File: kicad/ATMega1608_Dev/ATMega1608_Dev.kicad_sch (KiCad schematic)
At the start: 36 parts, among them J1 Alt Power, J2 USB_B_Micro, J3 Power OUT, J4 Comm, J5 GPIO1, J6 GPIO2, SW1 RESET, U1 MCP1700-3302E_SOT23, U2 FT232RQ, U3 ATMega1608_32

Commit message: Schematic complete
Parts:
- added H1, H2: MountingHole, MountingHole:MountingHole_2.7mm_M2.5, symbol Mechanical:MountingHole
- added LG1, LG2: logo, mech:MyBasic_rounded_50_1, symbol mech:logo
- added LG3: logo, Symbol:KiCad-Logo_5mm_SilkScreen, symbol mech:logo
- C7: renamed from C4; value C -> 100nF
- C8: renamed from C3; value C -> 100nF
- D5: renamed from D1; value D -> PESD3V3S1UB; footprint (none) -> Diode_SMD:D_SOD-523
- R2, R7, R8: value R -> 270Ω
- R9: renamed from R1; value R -> 10kΩ
- renumbered C5 to C1, C6 to C2, C7 to C3, C8 to C4, C1 to C5, C2 to C6, D2 to D1, D4 to D2, D5 to D4, J4 to J3, J5 to J4, J6 to J5, J3 to J6, R11 to R1, R9 to R10, R10 to R11
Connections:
- net +5V: now reaches C5.1, D1.1 (K), D2.1 (K), U1.3 (VI)
- net +3.3V renamed +3V3
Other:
- note added: "5mA"
- moved on the sheet: C1, C2, C3, C4, C5, C6, C7, C8, D1, D2, D3, D4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

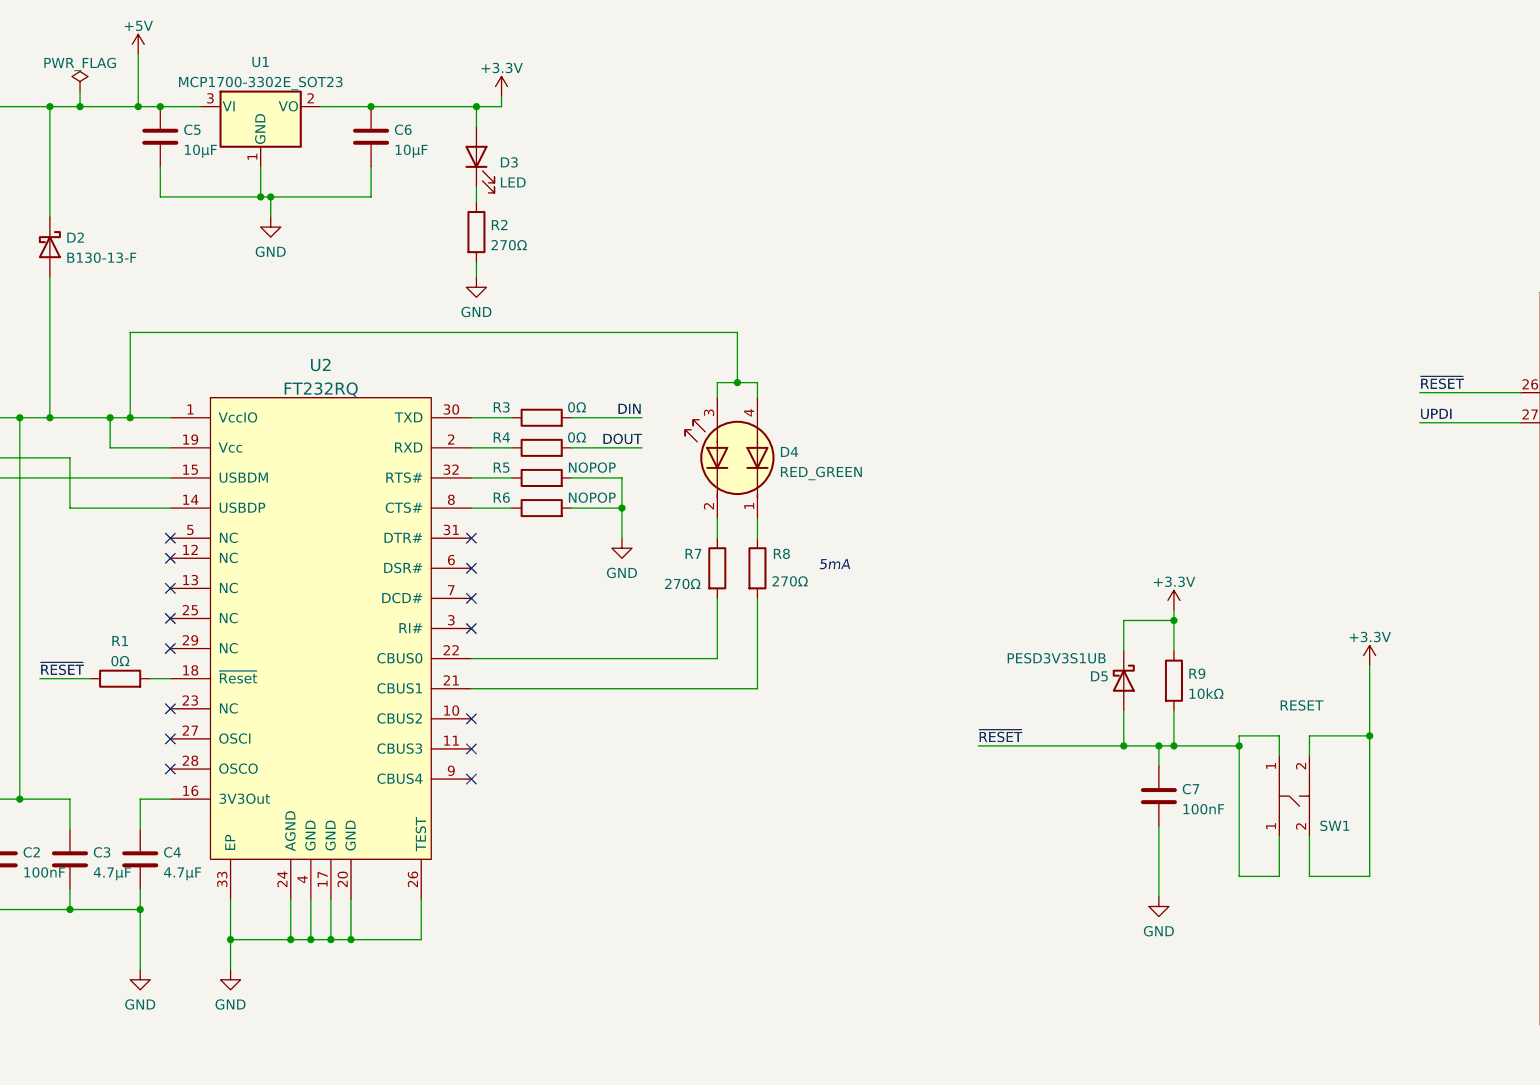
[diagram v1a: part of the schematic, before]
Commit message: Started on the layout
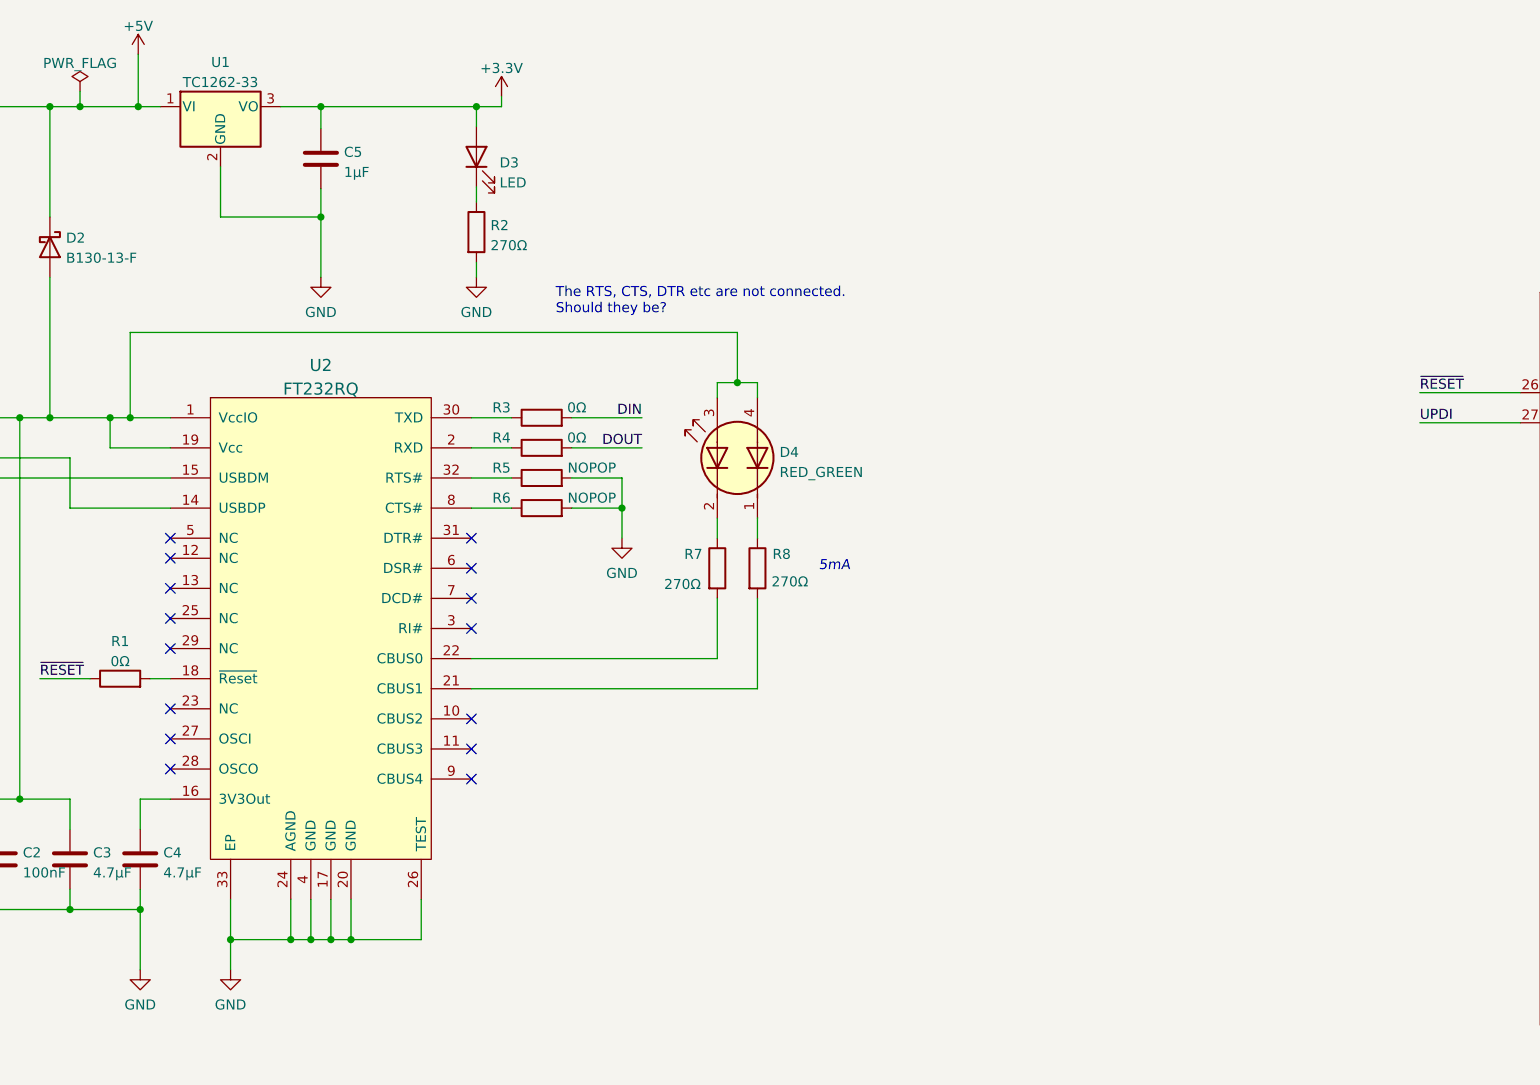
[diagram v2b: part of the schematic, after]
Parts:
- removed C6: 10μF, Capacitor_SMD:C_1210_3225Metric, symbol Device:C
- removed C7: 100nF, Capacitor_SMD:C_0805_2012Metric, symbol Device:C
- removed D5: PESD3V3S1UB, Diode_SMD:D_SOD-523, symbol Device:D_Schottky
- removed R9: 10kΩ, Resistor_SMD:R_0805_2012Metric, symbol Device:R
- removed SW1: RESET, Button_Switch_SMD:SW_SPST_Omron_B3FS-100xP, symbol attiny13_breakout:B3S-1000
- removed U1: MCP1700-3302E_SOT23, Package_TO_SOT_SMD:SOT-23, symbol Regulator_Linear:MCP1700-3302E_SOT23
- added U1: TC1262-33, Package_TO_SOT_SMD:SOT-223-3_TabPin2, symbol Regulator_Linear:TC1262-33
- C5: value 10μF -> 1μF; footprint Capacitor_SMD:C_1210_3225Metric -> Capacitor_SMD:C_0805_2012Metric_Pad1.18x1.45mm_HandSolder
- D4: footprint LED_SMD:LED_1210_3225Metric -> atmega1608_footprints:LED_KKAA_15-22SURSYGC
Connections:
- net +3V3: now also C5.1, U1.3 (VO)
- net +5V: now also U1.1 (VI); no longer C5.1
- net GND: now also U1.2 (GND)
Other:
- note added: "The RTS, CTS, DTR etc are not connected. Should they be?"

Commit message: The layout is complete - pending verification of USB interface
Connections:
- net DIN: now also J4.1 (Pin_1); no longer J4.2 (Pin_2)
- net DOUT: now also J4.2 (Pin_2); no longer J4.1 (Pin_1)
- net PF0: now also J5.10 (Pin_10); no longer J5.5 (Pin_5)
- net PF1: now also J5.9 (Pin_9); no longer J5.6 (Pin_6)
- net PF2: now also J5.8 (Pin_8); no longer J5.7 (Pin_7)
- net PF3: now also J5.7 (Pin_7); no longer J5.8 (Pin_8)
- net PF4: now also J5.6 (Pin_6); no longer J5.9 (Pin_9)
- net PF5: now also J5.5 (Pin_5); no longer J5.10 (Pin_10)
- net RxD0: now also J3.2 (Pin_2); no longer J3.4 (Pin_4)
- net SCL: now also J3.4 (Pin_4); no longer J3.2 (Pin_2)
- net SDA: now also J3.3 (Pin_3); no longer J3.1 (Pin_1)
- net TxD0: now also J3.1 (Pin_1); no longer J3.3 (Pin_3)
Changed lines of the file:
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@@
     (stroke (width 0) (type default) (color 0 0 0 0))
   )
-  (wire (pts (xy 165.227 193.675) (xy 174.752 193.675))
+  (wire (pts (xy 165.227 193.548) (xy 174.752 193.548))
     (stroke (width 0) (type default) (color 0 0 0 0))
   )
@@
     (stroke (width 0) (type default) (color 0 0 0 0))
   )
-  (wire (pts (xy 165.227 186.055) (xy 174.752 186.055))
+  (wire (pts (xy 165.227 185.928) (xy 174.752 185.928))
     (stroke (width 0) (type default) (color 0 0 0 0))
   )
@@
     (stroke (width 0) (type default) (color 0 0 0 0))
   )
-  (wire (pts (xy 165.227 198.755) (xy 174.752 198.755))
+  (wire (pts (xy 165.227 198.628) (xy 174.752 198.628))
     (stroke (width 0) (type default) (color 0 0 0 0))
   )
@@
     (stroke (width 0) (type default) (color 0 0 0 0))
   )
-  (wire (pts (xy 165.227 188.595) (xy 174.752 188.595))
+  (wire (pts (xy 165.227 188.468) (xy 174.752 188.468))
     (stroke (width 0) (type default) (color 0 0 0 0))
   )
@@
     (stroke (width 0) (type default) (color 0 0 0 0))
   )
-  (wire (pts (xy 165.227 180.975) (xy 174.752 180.975))
+  (wire (pts (xy 165.227 180.848) (xy 174.752 180.848))
     (stroke (width 0) (type default) (color 0 0 0 0))
   )
@@
     (stroke (width 0) (type default) (color 0 0 0 0))
   )
-  (wire (pts (xy 165.227 183.515) (xy 174.752 183.515))
+  (wire (pts (xy 165.227 183.388) (xy 174.752 183.388))
     (stroke (width 0) (type default) (color 0 0 0 0))
   )
@@
     (stroke (width 0) (type default) (color 0 0 0 0))
   )
-  (wire (pts (xy 165.227 191.135) (xy 174.752 191.135))
+  (wire (pts (xy 165.227 191.008) (xy 174.752 191.008))
     (stroke (width 0) (type default) (color 0 0 0 0))
   )
@@
     (stroke (width 0) (type default) (color 0 0 0 0))
   )
-  (wire (pts (xy 165.227 196.215) (xy 174.752 196.215))
+  (wire (pts (xy 165.227 196.088) (xy 174.752 196.088))
     (stroke (width 0) (type default) (color 0 0 0 0))
   )
@@
     (effects (font (size 1.27 1.27)) (justify right bottom))
   )
-  (label "SDA" (at 174.752 180.975 180)
-    (effects (font (size 1.27 1.27)) (justify right bottom))
-  )
-  (label "SS" (at 174.752 198.755 180)
+  (label "SDA" (at 174.752 185.928 180)
+    (effects (font (size 1.27 1.27)) (justify right bottom))
+  )
+  (label "SS" (at 174.752 198.628 180)
     (effects (font (size 1.27 1.27)) (justify right bottom))
   )
@@
     (effects (font (size 1.27 1.27)) (justify right bottom))
   )
-  (label "PF2" (at 174.752 246.38 180)
-    (effects (font (size 1.27 1.27)) (justify right bottom))
-  )
-  (label "PF1" (at 174.752 243.84 180)
-    (effects (font (size 1.27 1.27)) (justify right bottom))
-  )
-  (label "DIN" (at 174.752 210.82 180)
+  (label "PF2" (at 174.752 248.92 180)
+    (effects (font (size 1.27 1.27)) (justify right bottom))
+  )
+  (label "PF1" (at 174.752 251.46 180)
+    (effects (font (size 1.27 1.27)) (justify right bottom))
+  )
+  (label "DIN" (at 174.752 208.28 180)
     (effects (font (size 1.27 1.27)) (justify right bottom))
   )
@@
     (effects (font (size 1.27 1.27)) (justify right bottom))
   )
-  (label "MISO" (at 174.752 193.675 180)
-    (effects (font (size 1.27 1.27)) (justify right bottom))
-  )
-  (label "PF4" (at 174.752 251.46 180)
+  (label "MISO" (at 174.752 193.548 180)
+    (effects (font (size 1.27 1.27)) (justify right bottom))
+  )
+  (label "PF4" (at 174.752 243.84 180)
     (effects (font (size 1.27 1.27)) (justify right bottom))
   )
@@
     (effects (font (size 1.27 1.27)) (justify right bottom))
   )
-  (label "PF0" (at 174.752 241.3 180)
+  (label "PF0" (at 174.752 254 180)
     (effects (font (size 1.27 1.27)) (justify right bottom))
   )
@@
     (effects (font (size 1.27 1.27)) (justify right bottom))
   )
-  (label "TxD0" (at 174.752 186.055 180)
-    (effects (font (size 1.27 1.27)) (justify right bottom))
-  )
-  (label "SCL" (at 174.752 183.515 180)
+  (label "TxD0" (at 174.752 180.848 180)
+    (effects (font (size 1.27 1.27)) (justify right bottom))
+  )
+  (label "SCL" (at 174.752 188.468 180)
     (effects (font (size 1.27 1.27)) (justify right bottom))
   )
@@
     (effects (font (size 1.27 1.27)) (justify right bottom))
   )
-  (label "SCK" (at 174.752 196.215 180)
+  (label "SCK" (at 174.752 196.088 180)
     (effects (font (size 1.27 1.27)) (justify right bottom))
   )
@@
     (effects (font (size 1.27 1.27)) (justify right bottom))
   )
-  (label "PF3" (at 174.752 248.92 180)
+  (label "PF3" (at 174.752 246.38 180)
     (effects (font (size 1.27 1.27)) (justify right bottom))
   )
@@
     (effects (font (size 1.27 1.27)) (justify right bottom))
   )
-  (label "DOUT" (at 174.752 208.28 180)
+  (label "DOUT" (at 174.752 210.82 180)
     (effects (font (size 1.27 1.27)) (justify right bottom))
   )
@@
     (effects (font (size 1.27 1.27)) (justify right bottom))
   )
-  (label "RxD0" (at 174.752 188.595 180)
+  (label "RxD0" (at 174.752 183.388 180)
     (effects (font (size 1.27 1.27)) (justify right bottom))
   )
@@
     (effects (font (size 1.27 1.27)) (justify right bottom))
   )
-  (label "MOSI" (at 174.752 191.135 180)
+  (label "MOSI" (at 174.752 191.008 180)
     (effects (font (size 1.27 1.27)) (justify right bottom))
   )
@@
     (effects (font (size 1.27 1.27)) (justify right bottom))
   )
-  (label "PF5" (at 174.752 254 180)
+  (label "PF5" (at 174.752 241.3 180)
     (effects (font (size 1.27 1.27)) (justify right bottom))
   )
@@
     (pin "2")
   )
-  (symbol (lib_id "Connector:Conn_01x08_Male") (at 160.147 188.595 0) (unit 1)
+  (symbol (lib_id "Connector:Conn_01x08_Male") (at 160.147 188.468 0) (unit 1)
     (in_bom yes) (on_board yes)
-    (property "Reference" "J3" (id 0) (at 161.417 200.66 0))
-    (property "Value" "Comm" (id 1) (at 156.337 180.975 0))
-    (property "Footprint" "Connector_PinHeader_2.54mm:PinHeader_1x08_P2.54mm_Vertical" (id 2) (at 160.147 188.595 0)
-      (effects (font (size 1.27 1.27)) hide)
-    )
-    (property "Datasheet" "~" (id 3) (at 160.147 188.595 0)
-      (effects (font (size 1.27 1.27)) hide)
-    )
+    (property "Reference" "J3" (id 0) (at 161.417 200.533 0))
+    (property "Value" "Comm" (id 1) (at 156.337 180.848 0))
+    (property "Footprint" "Connector_PinHeader_2.54mm:PinHeader_1x08_P2.54mm_Vertical" (id 2) (at 160.147 188.468 0)
+      (effects (font (size 1.27 1.27)) hide)
+    )
+    (property "Datasheet" "~" (id 3) (at 160.147 188.468 0)
+      (effects (font (size 1.27 1.27)) hide)
+    )
